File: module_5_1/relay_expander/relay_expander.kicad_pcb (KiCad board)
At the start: 2 copper layers, 50.8 x 79.2 mm, 47 parts, among them J1 PLS-4, J2 2EDGR-5.08-05P, J3 2EDGR-5.08-04P, J4 2EDGR-5.08-02P, J5 2EDGR-5.08-02P, K1 HF49FD/024-1H12, K2 HF49FD/024-1H12, K3 HF49FD/024-1H12, K4 HF49FD/024-1H12, K5 HF49FD/024-1H12, K6 HF49FD/024-1H12, K7 HF49FD/024-1H12, Q1 AO3401A, U1 STM32G030F6Px, U2 ULN2003A, U3 MP1584, U4 AMS1117-3.3, U5 MAX3078E

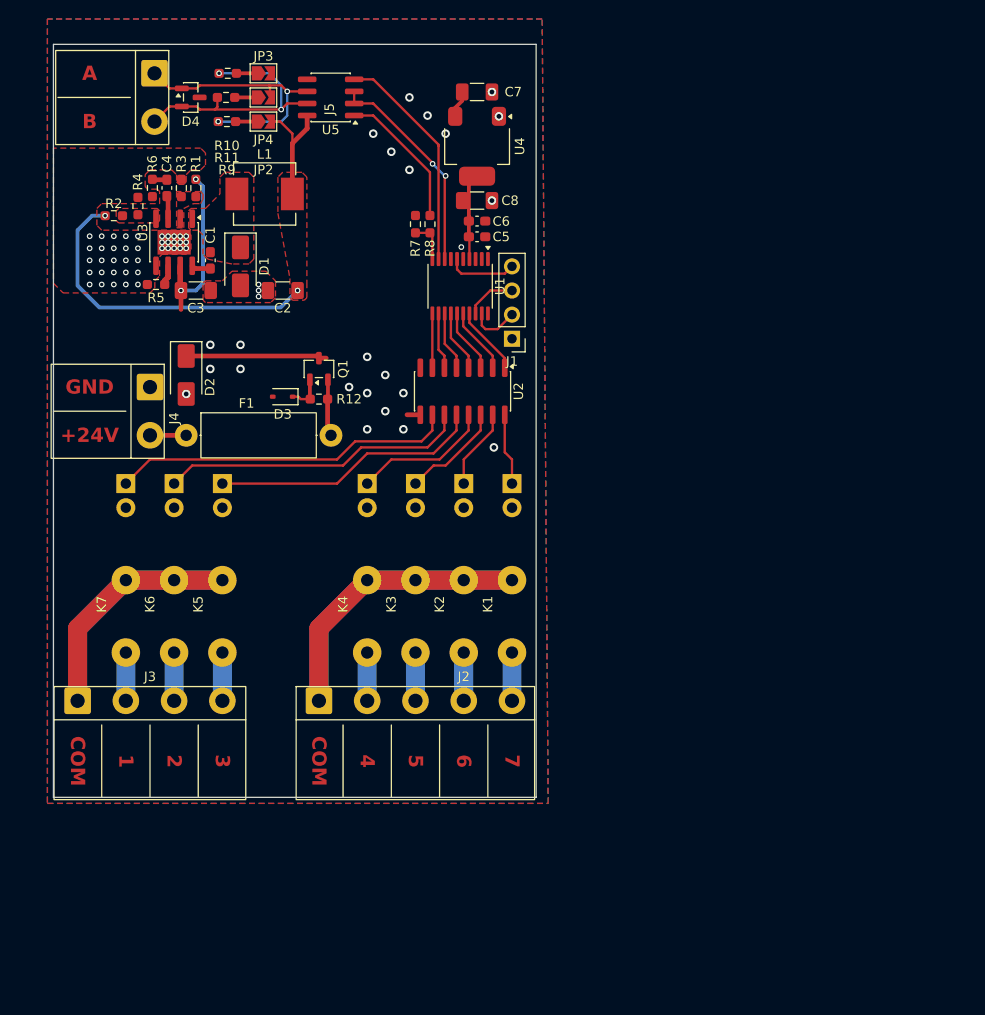
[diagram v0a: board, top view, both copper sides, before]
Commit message: PCB has been traced. Tiny improvements: * big capacitor on power input; * power indicating LED;
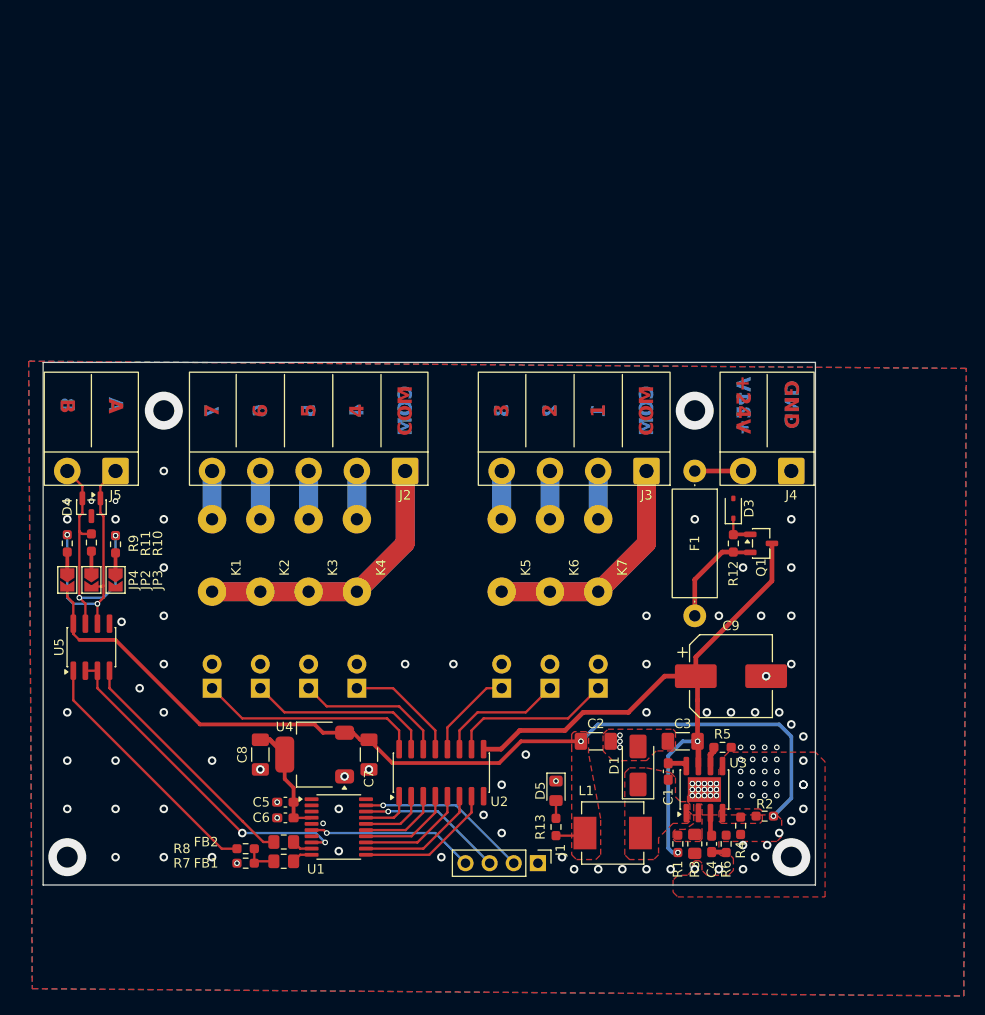
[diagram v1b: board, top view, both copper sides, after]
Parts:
- removed D2: SMAJ28A, Diode_SMD:D_SMA
- added C9: 220uF, Capacitor_SMD:CP_Elec_8x10.5, F.Cu at (201.9, 88.9)
- added D5: LED, LED_SMD:LED_0805_2012Metric_Pad1.15x1.40mm_HandSolder, F.Cu at (183.5, 101.0)
- added FB1: FerriteBead_Small, Capacitor_SMD:C_0805_2012Metric_Pad1.18x1.45mm_HandSolder, F.Cu at (154.9, 108.4)
- added FB2: FerriteBead_Small, Capacitor_SMD:C_0805_2012Metric_Pad1.18x1.45mm_HandSolder, F.Cu at (154.9, 106.4)
- added R13: 560, Resistor_SMD:R_0603_1608Metric_Pad0.98x0.95mm_HandSolder, F.Cu at (183.5, 104.8)
- R3: footprint Resistor_SMD:R_0603_1608Metric_Pad0.98x0.95mm_HandSolder -> Resistor_SMD:R_0805_2012Metric_Pad1.20x1.40mm_HandSolder
- moved R2 93.2 mm to (205.5, 103.6), turned to 0 degrees
- moved R6 91.7 mm to (201.4, 106.6), turned to -90 degrees
- moved R4 91.0 mm to (202.9, 104.6), turned to -90 degrees
- moved C4 89.7 mm to (199.9, 106.6), turned to -90 degrees
- moved R3 87.7 mm to (198.1, 106.6), turned to 90 degrees
- moved R1 85.7 mm to (196.3, 106.6), turned to 90 degrees
- moved U3 80.2 mm to (199.1, 100.8), turned to 90 degrees
- moved R5 77.0 mm to (201.0, 96.4), turned to 180 degrees
- moved L1 76.6 mm to (189.5, 105.4), turned to 180 degrees
- moved C1 72.2 mm to (195.3, 98.9), turned to -90 degrees
- moved C7 70.7 mm to (163.8, 97.2), turned to -90 degrees
- moved C3 69.8 mm to (196.8, 95.8), turned to 0 degrees
- moved R7 69.6 mm to (150.9, 108.6), turned to 0 degrees
- moved R8 68.5 mm to (150.9, 107.1), turned to 180 degrees
- moved J4 68.1 mm to (208.3, 67.3), turned to 180 degrees
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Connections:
- U1 pad 10: /RX -> Net-(U1-PA3)
- U1 pad 9: /TX -> Net-(U1-PA2)
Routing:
- net +5V: track 49.9 -> 101.0 mm
- net +24V: track 34.8 -> 68.4 mm
- net Net-(U2-O6): track 32.4 -> 13.3 mm
- net Net-(U2-O7): track 36.2 -> 17.1 mm
- net Net-(U2-O5): track 28.6 -> 9.71 mm
- net Net-(U2-O1): track 7.56 -> 23.5 mm
- net /SCLK: track 5.24 -> 18.1 mm, vias 0 -> 1
- net /DE: track 22.9 -> 35.2 mm
- net Net-(U5-RO): track 15.0 -> 26.8 mm
- net Net-(U2-O2): track 8.50 -> 19.7 mm
- net /NRST: track 7.37 -> 17.6 mm, vias 0 -> 1
- net /SDIO: track 5.34 -> 15.3 mm, vias 0 -> 1
- net Net-(U1-PA4): track 5.71 -> 14.7 mm
- net Net-(U1-PA5): track 5.97 -> 13.1 mm
- net Net-(U1-PA6): track 6.23 -> 11.6 mm
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- added copper zone on F.Cu, net Net-(D1-K)
- removed copper zone on F.Cu, net Net-(D4-A1)
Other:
- board size 50.8 x 79.2 mm -> 81.3 x 55 mm

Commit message: Gournd planes on DC-DC convertor have been fixed. Labels have been placed to be seen. An easter egg has been added.
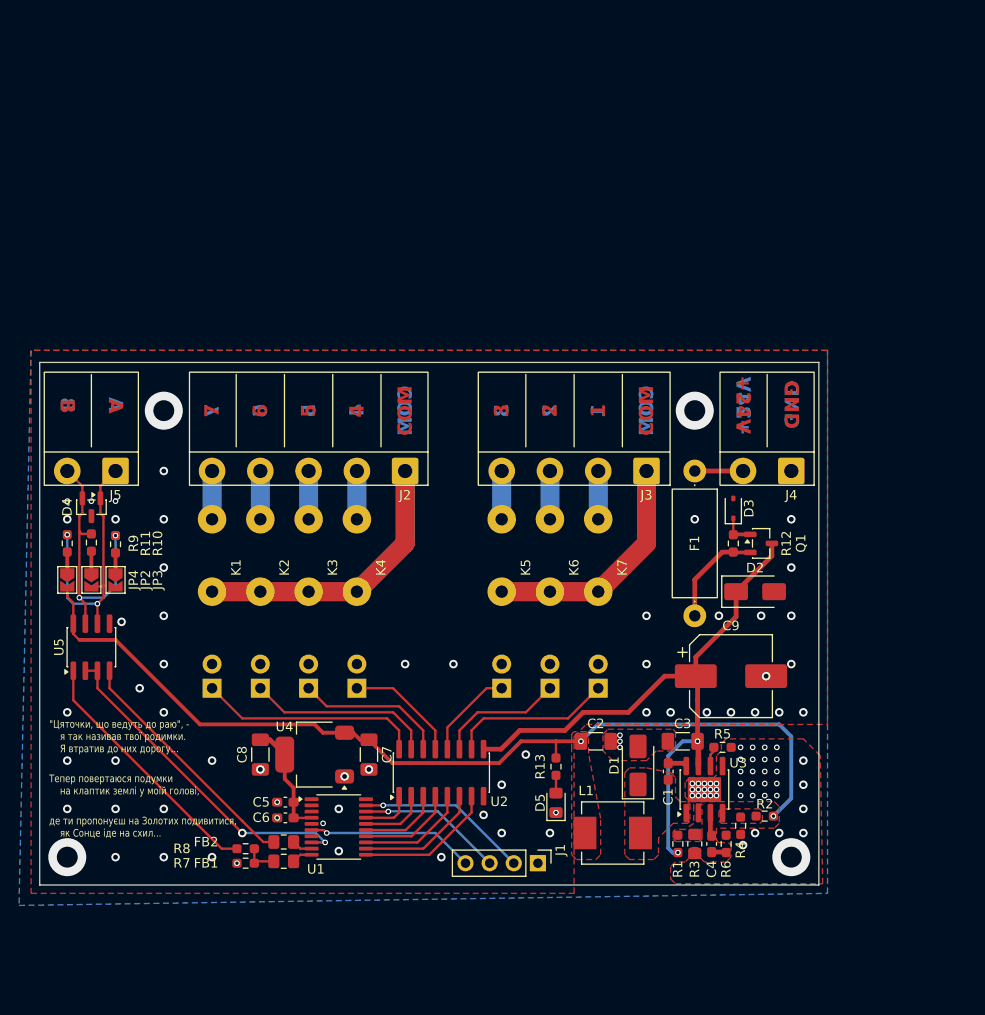
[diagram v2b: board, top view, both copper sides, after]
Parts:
- added D2: SMAJ28A, Diode_SMD:D_SMA, F.Cu at (204.5, 80.0)
- moved R13 6.35 mm to (183.5, 98.4), turned to 90 degrees
- moved D5 1.27 mm to (183.5, 102.2), turned to 90 degrees
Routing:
- net +5V: track 101.0 -> 100.0 mm
- net GND: vias 114 -> 103
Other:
- board size 81.3 x 55 mm -> 82 x 55 mm
- board text added: "{dblquote}Цяточки, що ведуть до раю{dblquote}, - я так називав твої родимки. Я втратив до них дорогу..."
- board text added: "Тепер повертаюся подумки на клаптик землі у моїй голові,"
- board text added: "де ти пропонуєш на Золотих подивитися, як Сонце іде на схил..."
